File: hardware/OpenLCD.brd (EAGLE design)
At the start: 45.7 x 30.5 mm, 33 parts, among them Q1 PNP, Q2 PNP, Q3 PNP, U1 MIC5219, U2 ATMEGA328P_TQFP, Y1 8MHz

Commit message: Board layout complete
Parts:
- removed C2, C5: 22pF, SparkFun-Capacitors:0603-CAP
- removed JP8: RESET, SparkFun-Connectors:1X01
- removed Y1: 8MHz, SparkFun-FreqCtrl:CRYSTAL-SMD-5X3
- added JP6: RESET, SparkFun-Connectors:1X01
- added R3: 10K, SparkFun-Resistors:0603-RES
- added Y2: 8MHz, SparkFun-FreqCtrl:RESONATOR-SMD
- C13, C19: device SparkFun:EIA3216 -> SparkFun-Capacitors:EIA3216
- Q1, Q2, Q3: value PNP -> PNP-500mA
- U1: value MIC5219 -> ATMEGA328P_TQFP; device SparkFun:SOT23-5 -> SparkFun-DigitalIC:TQFP32-08
- U2: value ATMEGA328P_TQFP -> MIC5219; device SparkFun-DigitalIC:TQFP32-08 -> SparkFun-PowerIC:SOT23-5
- moved LOGO4 28.7 mm to (3.30, 21.2)
- moved U$4 19.1 mm to (5.08, 5.08), flipped to the bottom
- moved U1 17.3 mm to (22.9, 16.5), turned to 315 degrees
- moved U2 17.3 mm to (6.35, 11.4), turned to 180 degrees
- moved R2 1.27 mm to (33.0, 24.1)
- moved LOGO3 0.25 mm to (16.9, 6.73)
- renumbered JP16 to JP5, JP17 to JP4, JP9 to JP3, SJ3 to SJ2, SJ4 to SJ1
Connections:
- removed net E: JP5.1, U2.25
- new net EN: JP5.1, U1.25
- net !SS: now also R3.1, U1.14; no longer U2.14
- net A6: now also U1.19; no longer U2.19
- net A7: now also U1.22; no longer U2.22
- net AREF: now also U1.20; no longer U2.20
- net BL-B: now also U1.13; no longer U2.13
- net BL-G: now also U1.10; no longer U2.10
- net BL-R/W: now also U1.9; no longer U2.9
- net D4: now also U1.26; no longer U2.26
- net D5: now also U1.32; no longer U2.32
- net D6: now also U1.1; no longer U2.1
- net D7: now also U1.2; no longer U2.2
- net GND: now also U1.21, U1.3, U1.5, U2.2, Y2.2; no longer C2.1, C5.1, U1.2, U2.21, U2.3, U2.5
- net N$2: now also U1.8, Y2.3; no longer C2.2, U2.7, Y1.3
- net N$3: now also U1.7, Y2.1; no longer C5.2, U2.8, Y1.1
- net R/W: now also U1.24; no longer U2.24
- net RAW: now also U2.1, U2.3; no longer U1.1, U1.3
- net RS: now also U1.23; no longer U2.23
- net RST: now also JP6.1, U1.29; no longer JP8.1, U2.29
- net RXI: now also U1.30; no longer U2.30
- net SCK: now also U1.17; no longer U2.17
- net SCL: now also U1.28; no longer U2.28
- net SDA: now also U1.27; no longer U2.27
- net SDI: now also U1.15; no longer U2.15
- net SDO: now also U1.16; no longer U2.16
- net TXO: now also U1.31; no longer U2.31
- net VCC: now also R3.2, U1.18, U1.4, U1.6, U2.5; no longer U1.5, U2.18, U2.4, U2.6
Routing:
- net EN: track 0.00 -> 13.2 mm
- net VCC: track 75.0 -> 87.5 mm
- net E: track 10.6 -> 0.00 mm
- net GND: track 0.00 -> 5.82 mm, vias 5 -> 10
- net BL-B: track 20.2 -> 24.8 mm
- net N$2: track 6.47 -> 2.13 mm
- net SCK: track 7.47 -> 11.4 mm
- net RST: track 17.9 -> 21.6 mm, vias 1 -> 2
- net RXI: track 59.0 -> 62.6 mm
- net N$3: track 4.99 -> 2.11 mm
- net D6: track 13.7 -> 11.0 mm, vias 1 -> 0
- net D4: track 16.3 -> 19.0 mm
- net SCL: track 21.7 -> 24.1 mm
- net D7: track 16.8 -> 19.2 mm
- net !SS: track 9.73 -> 12.0 mm
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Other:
- board text added: "Contrast"
- board text added: "SerLCD"
- board text removed: "0.15"
- board text removed: "0.7173"
- board text removed: "1.0236"
- board text removed: "1.20"
- board text removed: "1.30"
- board text removed: "1.40"
- board text removed: "1.50"
- board text removed: "CNT"
- board text removed: "OpenLCD"

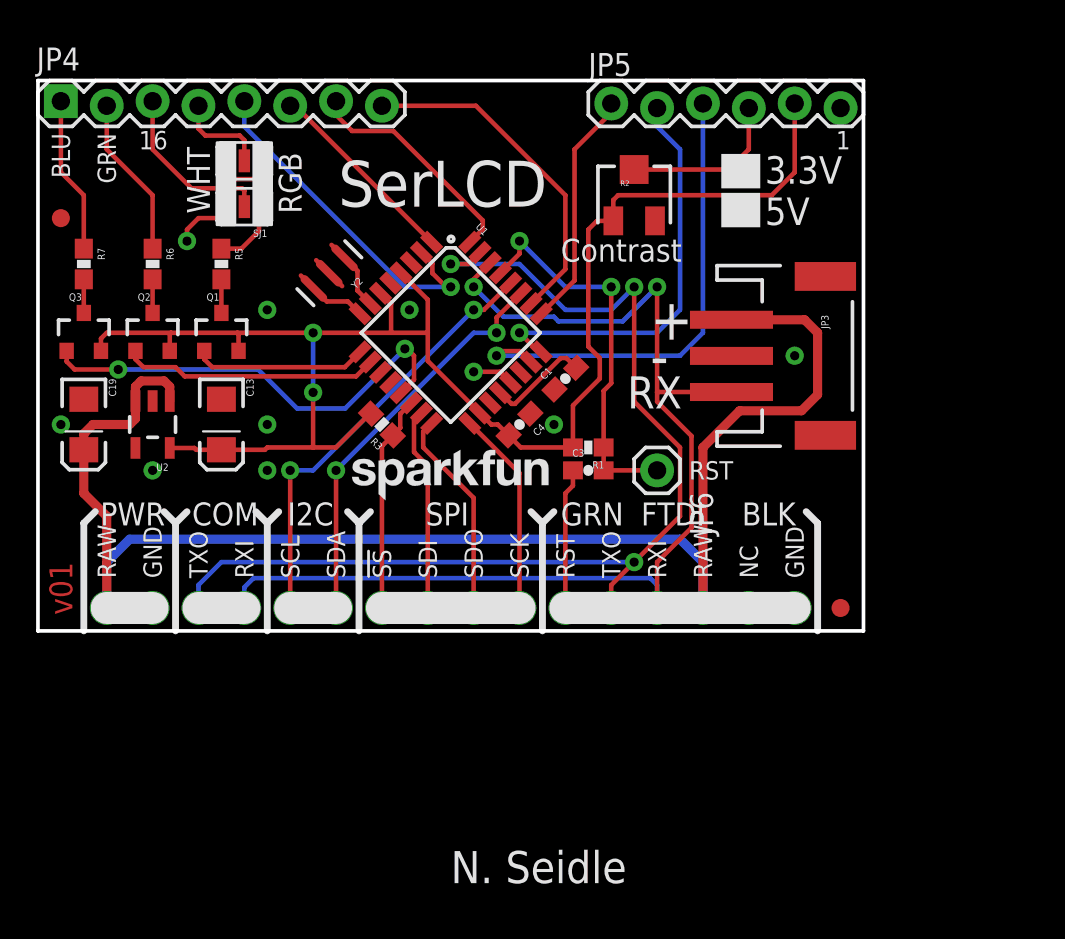
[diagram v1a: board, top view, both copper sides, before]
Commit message: Adding jumpers for size and voltage.
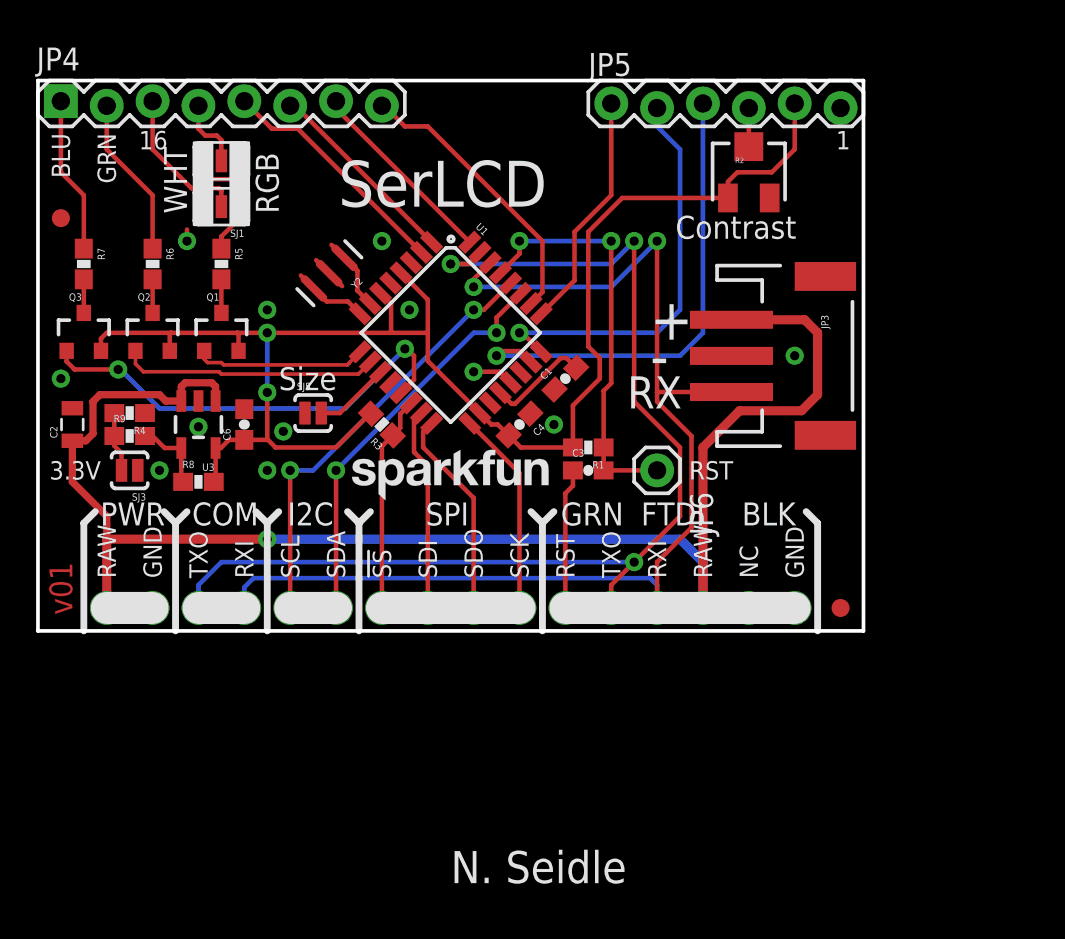
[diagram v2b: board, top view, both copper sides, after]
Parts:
- removed C13, C19: 10uF, SparkFun-Capacitors:EIA3216
- removed U2: MIC5219, SparkFun-PowerIC:SOT23-5
- added C2: 1.0uF/25V, SparkFun-Capacitors:0805
- added C6: 2.2uF, SparkFun-Capacitors:0603-CAP
- added R4: 330, SparkFun-Resistors:0603-RES
- added R8: 240, SparkFun-Resistors:0603-RES
- added R9: 390, SparkFun-Resistors:0603-RES
- added SJ3: VSET, SparkFun-Passives:PAD-JUMPER-2-NO_YES_SILK
- added SJ5: Size, SparkFun-Passives:PAD-JUMPER-2-NO_YES_SILK
- added U3: MIC5205-ADJ, SparkFun-PowerIC:SOT23-5
- moved R2 6.48 mm to (39.4, 25.4)
- moved SJ1 1.27 mm to (10.2, 23.5)
- moved SJ2 1.27 mm to (10.2, 26.0)
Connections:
- removed net A6: U1.19
- removed net A7: U1.22
- new net N$6: R8.1, R9.2, U3.4
- new net N$7: R4.2, R9.1, SJ3.2
- new net SIZE: SJ5.2, U1.11
- net GND: now also C2.2, C6.2, R4.1, SJ3.1, SJ5.1, U3.2; no longer C13.C, C19.C, U2.2
- net RAW: now also C2.1, U3.1, U3.3; no longer C19.A, U2.1, U2.3
- net VCC: now also C6.1, R8.2, U3.5; no longer C13.A, U2.5
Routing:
- net CONTRAST: track 9.10 -> 2.13 mm
- net D7: track 19.2 -> 13.3 mm, vias 1 -> 0
- net SIZE: track 0.00 -> 4.22 mm
- net N$6: track 0.00 -> 4.20 mm
- net N$7: track 0.00 -> 3.34 mm
- net D4: track 19.0 -> 15.7 mm
- net GND: track 5.82 -> 2.93 mm, vias 10 -> 12
- net RXI: track 62.6 -> 64.6 mm
- net D5: track 12.8 -> 10.9 mm
- net VCC: track 87.5 -> 85.7 mm
- net TXO: track 60.0 -> 61.4 mm
- net RST: track 21.6 -> 23.1 mm
- net BACKLIGHT2: track 9.58 -> 8.31 mm
- net BACKLIGHT1: track 5.22 -> 3.95 mm
- net A-RED/WHITE: track 7.79 -> 6.62 mm
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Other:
- board text added: "Size"
- board text removed: "5V"

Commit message: Standard I2C interface. I2C pull ups. VCC on FTDI connector.
Added silk to both sides. Moved contrast pin to PWM pin and direct
connect.
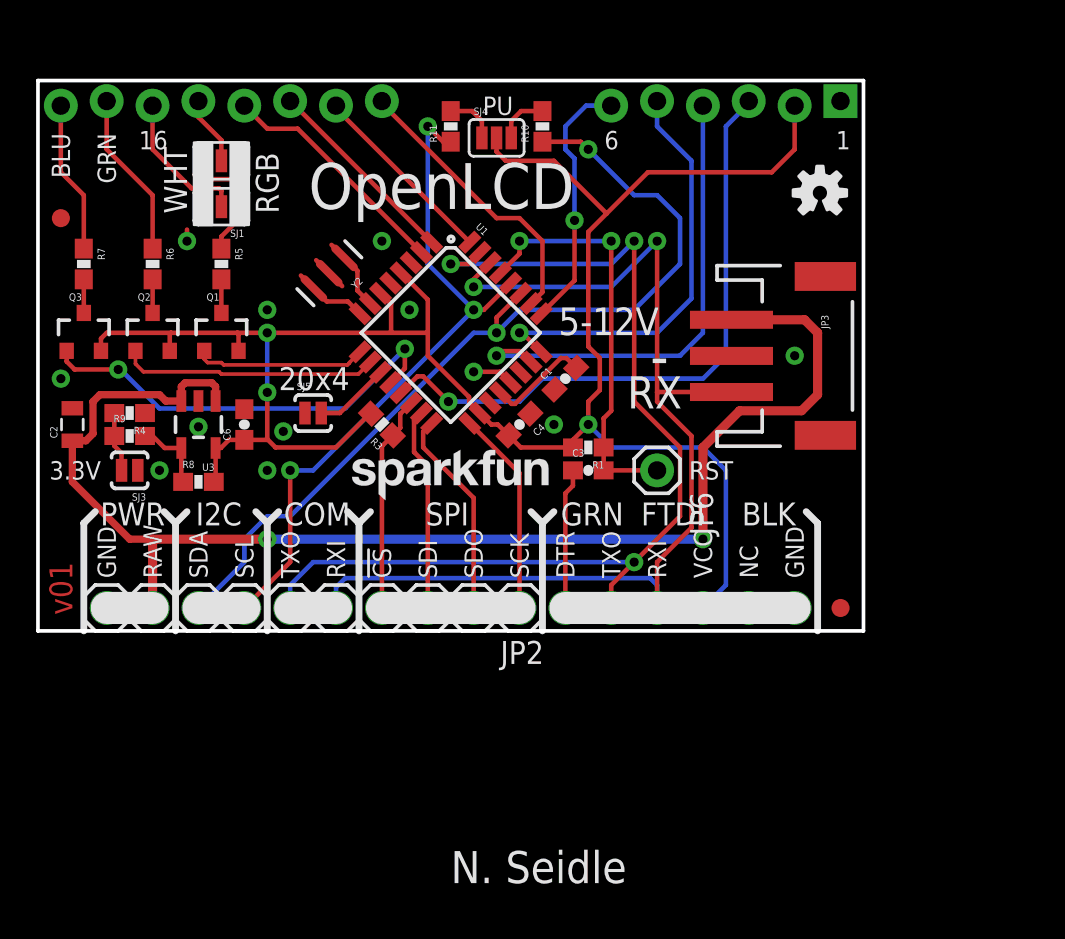
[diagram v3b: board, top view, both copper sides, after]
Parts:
- removed JP4: (no value), SparkFun-Connectors:1X08_LOCK
- removed JP5: (no value), SparkFun-Connectors:1X06-SIP_LOCK
- removed R2: 10K, SparkFun-Electromechanical:TRIMPOT-3MM-2
- added R10, R11: 4.7K, SparkFun-Resistors:0603-RES
- added SJ4: I2C-PU, SparkFun-Passives:PAD-JUMPER-3-NC_BY_PASTE_YES_SILK_FULL_BOX
- added U2: 4BIT-RGB, SparkFun-Displays:LCD-16X2_NOSILK-KIT-4BIT
- moved U$4 42.8 mm to (43.3, 24.3), flipped to the top
- flipped JP2 to the top, turned to 180 degrees
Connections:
- net !SS renamed !CS
- new net N$10: R10.2, SJ4.3
- new net N$9: R11.2, SJ4.1
- net A-BLUE: now also U2.18; no longer JP4.1
- net A-GREEN: now also U2.17; no longer JP4.2
- net BACKLIGHT1: now also U2.15; no longer JP4.4
- net BACKLIGHT2: now also U2.16; no longer JP4.3
- net BL-B: now also U1.12; no longer U1.13
- net CONTRAST: now also U1.13, U2.3; no longer JP5.4, R2.2
- net D4: now also U2.11; no longer JP4.8
- net D5: now also U2.12; no longer JP4.7
- net D6: now also U2.13; no longer JP4.6
- net D7: now also U2.14; no longer JP4.5
- net EN: now also U2.6; no longer JP5.1
- net GND: now also JP2.10, U2.1; no longer JP2.9, JP5.6, R2.3
- net R/W: now also U2.5; no longer JP5.2
- net RAW: now also JP2.9; no longer JP1.VCC, JP2.10
- net RS: now also U2.4; no longer JP5.3
- net RXI: now also JP2.5; no longer JP2.7
- net SCL: now also JP2.7, R11.1; no longer JP2.6
- net SDA: now also JP2.8, R10.1; no longer JP2.5
- net TXO: now also JP2.6; no longer JP2.8
- net VCC: now also JP1.VCC, SJ4.2, U2.2; no longer JP5.5, R2.1
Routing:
- net CONTRAST: track 2.13 -> 34.6 mm, vias 0 -> 1
- net SDA: track 22.4 -> 50.0 mm
- net VCC: track 85.7 -> 110.1 mm, vias 2 -> 3
- net SCL: track 24.1 -> 38.0 mm, vias 2 -> 3
- net RAW: track 83.0 -> 75.4 mm, vias 1 -> 2
- net TXO: track 61.4 -> 56.4 mm
- net RXI: track 64.6 -> 59.5 mm
- net N$9: track 0.00 -> 2.89 mm
- net N$10: track 0.00 -> 2.89 mm
- net EN: track 13.2 -> 14.4 mm, vias 0 -> 1
- net R/W: track 22.8 -> 23.7 mm
- net BL-B: track 24.8 -> 24.0 mm
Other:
- board text added: "!CS"
- board text added: "20x4"
- board text added: "5-12V"
- board text added: "6"
- board text added: "DTR"
- board text added: "OpenLCD"
- board text added: "PU"
- board text added: "VCC"
- board text removed: "!SS"
- board text removed: "+"
- board text removed: "Contrast"
- board text removed: "SerLCD"
- board text removed: "Size"

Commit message: Final touchup before QC review.
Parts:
- SJ3: value VSET -> 3.3V
- moved U$4 1.98 mm to (41.9, 22.9)
- moved SJ1 1.27 mm to (8.89, 23.5)
- moved SJ2 1.27 mm to (8.89, 26.0)
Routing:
- net RAW: track 75.4 -> 77.7 mm, vias 2 -> 1
- net RST: track 23.1 -> 25.1 mm
- net TXO: track 56.4 -> 57.6 mm
- net SDA: track 50.0 -> 50.9 mm, vias 2 -> 3
- net RXI: track 59.5 -> 60.3 mm
- net BACKLIGHT2: track 8.07 -> 7.54 mm
- net BACKLIGHT1: track 3.84 -> 3.31 mm
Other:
- board text added: "CTR"
- board text added: "D4"
- board text added: "D5"
- board text added: "D6"
- board text added: "EN"
- board text added: "RS"
- board text added: "RW"
- board text removed: "1"
- board text removed: "16"
- board text removed: "6"

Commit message: Resolved issue 1
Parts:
- added TP1, TP2: (no value), SparkFun-Passives:PAD.03X.04
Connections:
- net GND: now also JP1.CTS
- net N$7: now also TP1.P$1
- net SIZE: now also TP2.P$1
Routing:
- net SIZE: track 4.22 -> 9.15 mm, vias 0 -> 1
- net N$7: track 3.34 -> 7.75 mm, vias 0 -> 1
- net SCL: track 38.0 -> 38.7 mm
- net BL-B: track 24.0 -> 23.4 mm

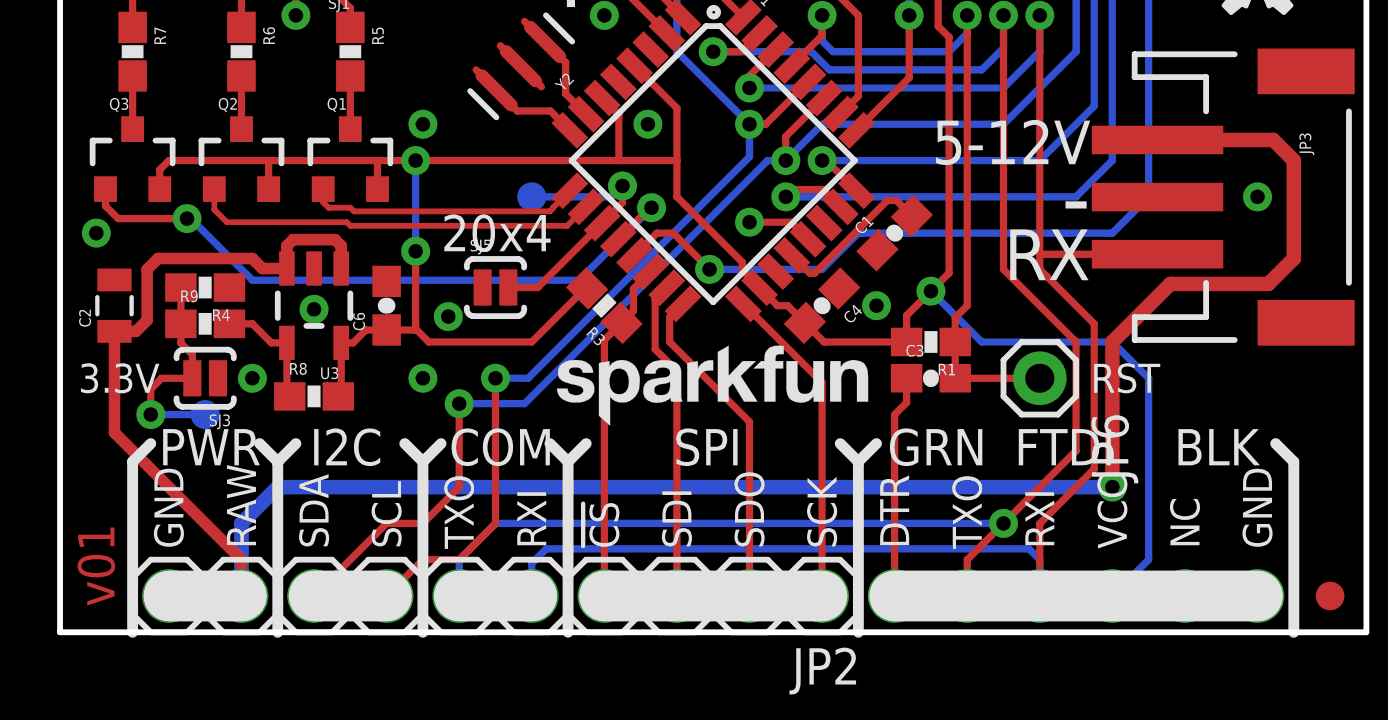
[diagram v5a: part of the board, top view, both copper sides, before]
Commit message: Correcting silk
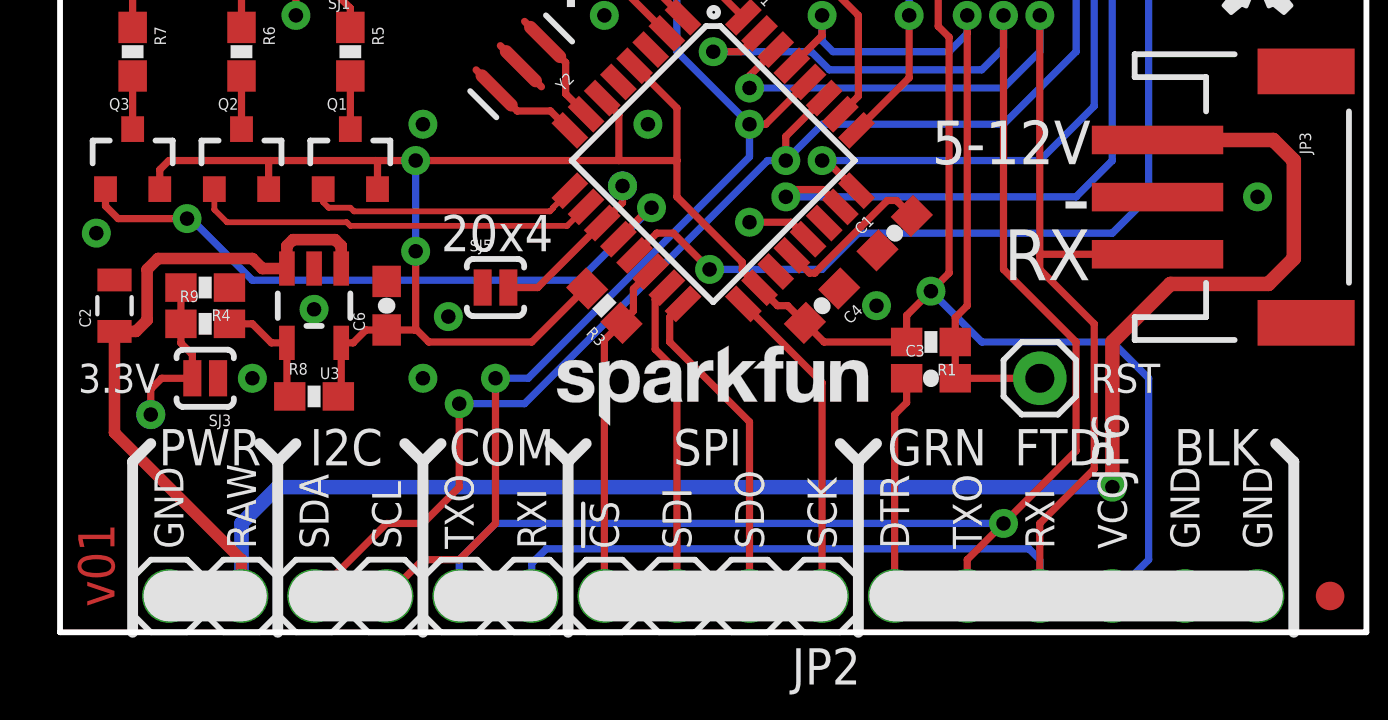
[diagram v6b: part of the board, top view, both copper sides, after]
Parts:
- moved TP2 3.20 mm to (19.7, 15.6)
- moved TP1 1.91 mm to (3.17, 7.62)
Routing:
- net SIZE: track 9.15 -> 5.81 mm
- net N$7: track 7.75 -> 5.84 mm
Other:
- board text removed: "NC"
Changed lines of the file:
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@@
 <text x="34.798" y="2.921" size="1.016" layer="21" font="vector" ratio="15" rot="R90">RXI</text>
 <text x="37.338" y="2.921" size="1.016" layer="21" font="vector" ratio="15" rot="R90">VCC</text>
-<text x="39.878" y="2.921" size="1.016" layer="21" font="vector" ratio="15" rot="R90">NC</text>
 <text x="42.418" y="2.921" size="1.016" layer="21" font="vector" ratio="15" rot="R90">GND</text>
 <polygon width="0.127" layer="21">
@@
 <text x="33.782" y="2.921" size="1.016" layer="22" font="vector" ratio="15" rot="MR90">RXI</text>
 <text x="36.322" y="2.921" size="1.016" layer="22" font="vector" ratio="15" rot="MR90">VCC</text>
-<text x="38.862" y="2.921" size="1.016" layer="22" font="vector" ratio="15" rot="MR90">NC</text>
 <text x="41.402" y="2.921" size="1.016" layer="22" font="vector" ratio="15" rot="MR90">GND</text>
 <text x="24.638" y="28.575" size="1.016" layer="21" font="vector" ratio="15">PU</text>
@@
 <text x="16.002" y="27.94" size="1.016" layer="21" font="vector" ratio="15" rot="R270">D5</text>
 <text x="13.462" y="27.94" size="1.016" layer="21" font="vector" ratio="15" rot="R270">D6</text>
+<text x="39.878" y="2.921" size="1.016" layer="21" font="vector" ratio="15" rot="R90">GND</text>
+<text x="38.862" y="2.921" size="1.016" layer="22" font="vector" ratio="15" rot="MR90">GND</text>
 </plain>
 <attributes>
@@
 </element>
 <element name="SJ4" library="SparkFun-Passives" package="PAD-JUMPER-3-NC_BY_PASTE_YES_SILK_FULL_BOX" value="I2C-PU" x="25.4" y="27.305"/>
-<element name="TP1" library="SparkFun-Passives" package="PAD.03X.04" value="" x="5.08" y="7.62" rot="MR0"/>
-<element name="TP2" library="SparkFun-Passives" package="PAD.03X.04" value="" x="16.51" y="15.24" rot="MR0"/>
+<element name="TP1" library="SparkFun-Passives" package="PAD.03X.04" value="" x="3.175" y="7.62" rot="MR0"/>
+<element name="TP2" library="SparkFun-Passives" package="PAD.03X.04" value="" x="19.685" y="15.621" rot="MR0"/>
 </elements>
 <signals>
@@
 <wire x1="19.685" y1="15.03205625" x2="19.685" y2="15.621" width="0.254" layer="1"/>
 <via x="19.685" y="15.621" extent="1-16" drill="0.508"/>
-<wire x1="19.685" y1="15.621" x2="19.304" y2="15.24" width="0.254" layer="16"/>
-<wire x1="19.304" y1="15.24" x2="16.51" y2="15.24" width="0.254" layer="16"/>
 </signal>
 <signal name="N$6">
@@
 <wire x1="4.23" y1="10.121" x2="4.63" y2="9.721" width="0.254" layer="1"/>
 <wire x1="4.63" y1="8.89" x2="4.63" y2="9.721" width="0.254" layer="1"/>
-<contactref element="TP1" pad="P$1"/>
 <via x="3.175" y="7.62" extent="1-16" drill="0.508"/>
-<wire x1="3.175" y1="7.62" x2="5.08" y2="7.62" width="0.254" layer="16"/>
 <wire x1="4.63" y1="8.89" x2="3.556" y2="8.89" width="0.254" layer="1"/>
 <wire x1="3.556" y1="8.89" x2="3.175" y2="8.509" width="0.254" layer="1"/>
 <wire x1="3.175" y1="8.509" x2="3.175" y2="7.62" width="0.254" layer="1"/>
+<contactref element="TP1" pad="P$1"/>
 </signal>
 <signal name="N$9">
